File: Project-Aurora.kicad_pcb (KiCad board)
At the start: 4 copper layers, 285 x 94.6 mm, 264 parts, among them P1 USB_OTG, P2 FLASH_HDR, SW1 Reset, SW10 SW_PUSH, SW11 SW_PUSH, SW12 SW_PUSH, SW13 SW_PUSH, SW14 SW_PUSH, SW15 SW_PUSH, SW16 SW_PUSH, SW17 SW_PUSH, SW18 SW_PUSH, SW19 SW_PUSH, SW2 SW_PUSH, SW20 SW_PUSH, SW21 SW_PUSH, SW22 SW_PUSH, SW23 SW_PUSH, SW24 SW_PUSH, SW25 SW_PUSH, SW26 SW_PUSH, SW27 SW_PUSH, SW28 SW_PUSH, SW29 SW_PUSH, SW3 SW_PUSH, SW30 SW_PUSH, SW31 SW_PUSH, SW32 SW_PUSH, SW33 SW_PUSH, SW34 SW_PUSH, SW35 SW_PUSH, SW36 SW_PUSH, SW37 SW_PUSH, SW38 SW_PUSH, SW39 SW_PUSH, SW4 SW_PUSH, SW40 SW_PUSH, SW41 SW_PUSH, SW42 SW_PUSH, SW43 SW_PUSH, SW44 SW_PUSH, SW45 SW_PUSH, SW46 SW_PUSH, SW47 SW_PUSH, SW48 SW_PUSH, SW49 SW_PUSH, SW5 SW_PUSH, SW50 SW_PUSH, SW51 SW_PUSH, SW52 SW_PUSH, SW53 SW_PUSH, SW54 SW_PUSH, SW55 SW_PUSH, SW56 SW_PUSH, SW57 SW_PUSH, SW58 SW_PUSH, SW59 SW_PUSH, SW6 SW_PUSH, SW60 SW_PUSH, SW61 SW_PUSH, SW62 SW_PUSH, SW63 SW_PUSH, SW64 SW_PUSH, SW65 SW_PUSH, SW66 SW_PUSH, SW7 SW_PUSH, SW8 SW_PUSH, SW9 SW_PUSH, U1 MK20DX256VLH7, U2 IS31FL3732, U3 IS31FL3732, U6 Case-Ground, X1 CRYSTAL_SMD

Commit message: Did some visual cleanup.
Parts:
- moved FID1 24.4 mm to (66.0, 83.8)
- moved FID2 24.4 mm to (66.0, 83.8)
- moved D126 10.9 mm to (321.1, 121.4), turned to 0 degrees
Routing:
- net /Keymatrix/Row4Col14: track 19.8 -> 4.89 mm
- net /Keymatrix/Row4: track 307.5 -> 296.7 mm
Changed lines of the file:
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@@
     (thickness 1.6002)
     (drawings 3814)
-    (tracks 2956)
+    (tracks 2954)
     (zones 0)
     (modules 264)
@@
   )
   (module Fiducials:Fiducial_1mm_Dia_2.54mm_Outer_CopperBottom (layer Front)
-    (at 90.424 83.82)
+    (at 66.04 83.82)
     (descr "Circular Fiducial, 1mm bare copper bottom; 2.54mm keepout")
     (tags marker)
@@
   )
   (module Fiducials:Fiducial_1mm_Dia_2.54mm_Outer_CopperTop (layer Front)
-    (at 90.424 83.82)
+    (at 66.04 83.82)
     (descr "Circular Fiducial, 1mm bare copper top; 2.54mm keepout")
     (tags marker)
@@
   (module Keyboard_Stuff:RGB (layer Front)
     (at 326.212 111.85 180)
-    (fp_text reference D1 (at -3.048 2.032 180) (layer F.SilkS)
+    (fp_text reference D1 (at 2.616 2.122 180) (layer F.SilkS)
       (effects (font (size 1 1) (thickness 0.125)))
     )
@@
   (module Keyboard_Stuff:RGB (layer Front)
     (at 161.544 154.874 180)
-    (fp_text reference D21 (at -1.016 3.236 180) (layer F.SilkS)
+    (fp_text reference D21 (at 0 7.046 180) (layer F.SilkS)
       (effects (font (size 1 1) (thickness 0.125)))
     )
@@
     (tags SOD-123)
     (attr smd)
-    (fp_text reference D89 (at 4.064 0 90) (layer F.SilkS)
+    (fp_text reference D89 (at -3.048 0 180) (layer F.SilkS)
       (effects (font (size 1 1) (thickness 0.15)))
     )
@@
     (tags SOD-123)
     (attr smd)
-    (fp_text reference D95 (at 4.064 0 90) (layer F.SilkS)
+    (fp_text reference D95 (at -0.254 -3.302 90) (layer F.SilkS)
       (effects (font (size 1 1) (thickness 0.15)))
     )
@@
     (tags SOD-123)
     (attr smd)
-    (fp_text reference D112 (at 4.064 0) (layer F.SilkS)
+    (fp_text reference D112 (at -4.318 0) (layer F.SilkS)
       (effects (font (size 1 1) (thickness 0.15)))
     )
@@
     (tags SOD-123)
     (attr smd)
-    (fp_text reference D119 (at 4.064 0 90) (layer F.SilkS)
+    (fp_text reference D119 (at -3.302 -1.016 180) (layer F.SilkS)
       (effects (font (size 1 1) (thickness 0.15)))
     )
@@
     (tags SOD-123)
     (attr smd)
-    (fp_text reference D124 (at 4.064 0) (layer F.SilkS)
+    (fp_text reference D124 (at 0.254 2.032) (layer F.SilkS)
       (effects (font (size 1 1) (thickness 0.15)))
     )
@@
   )
   (module Keyboard_Stuff:SOD-123 (layer Front)
-    (at 331.216 125.476 270)
+    (at 321.056 121.412)
     (descr SOD-123)
     (tags SOD-123)
     (attr smd)
-    (fp_text reference D126 (at 4.064 0 270) (layer F.SilkS)
+    (fp_text reference D126 (at 4.064 0) (layer F.SilkS)
       (effects (font (size 1 1) (thickness 0.15)))
     )
-    (fp_text value D (at 0 2.1 270) (layer F.Fab)
+    (fp_text value D (at 0 2.1) (layer F.Fab)
       (effects (font (size 1 1) (thickness 0.15)))
     )
@@
     (fp_line (start -2 0.9) (end 1.54 0.9) (layer F.SilkS) (width 0.15))
     (fp_line (start -2 -0.9) (end 1.54 -0.9) (layer F.SilkS) (width 0.15))
-    (pad 1 smd rect (at -1.635 0 270) (size 0.91 1.22) (layers Front F.Paste F.Mask)
+    (pad 1 smd rect (at -1.635 0) (size 0.91 1.22) (layers Front F.Paste F.Mask)
       (net 55 /Keymatrix/Row4))
-    (pad 2 smd rect (at 1.635 0 270) (size 0.91 1.22) (layers Front F.Paste F.Mask)
+    (pad 2 smd rect (at 1.635 0) (size 0.91 1.22) (layers Front F.Paste F.Mask)
       (net 124 /Keymatrix/Row4Col14))
   )
@@
   (module Keyboard_Stuff:RGB (layer Front)
     (at 314.306 111.85 180)
-    (fp_text reference D129 (at -3.048 2.032 180) (layer F.SilkS)
+    (fp_text reference D129 (at 4.426 2.122 180) (layer F.SilkS)
       (effects (font (size 1 1) (thickness 0.125)))
     )
@@
   (segment (start 147.574 99.933) (end 128.524 99.933) (width 0.19) (layer Front) (net 54) (status 30))
   (segment (start 128.524 99.933) (end 109.474 99.933) (width 0.19) (layer Front) (net 54) (status 30))
+  (segment (start 311.912 123.841) (end 316.992 123.841) (width 0.19) (layer Front) (net 55))
+  (segment (start 316.992 123.841) (end 319.421 121.412) (width 0.19) (layer Front) (net 55))
   (via (at 114.3 123.952) (size 0.6) (layers Front Back) (net 55))
   (segment (start 132.142 150.43) (end 137.156 150.43) (width 0.19) (layer Back) (net 55) (status 20))
@@
   (segment (start 105.156 140.716) (end 107.188 138.684) (width 0.19) (layer Front) (net 55))
   (segment (start 102.163 140.716) (end 105.156 140.716) (width 0.19) (layer Front) (net 55))
-  (segment (start 311.912 123.841) (end 331.216 123.841) (width 0.19) (layer Front) (net 55) (status 30))
   (segment (start 102.108 140.716) (end 102.163 140.716) (width 0.19) (layer Front) (net 55))
   (segment (start 276.352 123.841) (end 311.912 123.841) (width 0.19) (layer Front) (net 55) (status 30))
@@
   (segment (start 326.157 97.88) (end 324.469 99.568) (width 0.19) (layer Front) (net 123) (status 20))
   (segment (start 330.816 97.88) (end 326.157 97.88) (width 0.19) (layer Front) (net 123) (status 10))
-  (segment (start 332.121 127.111) (end 331.216 127.111) (width 0.19) (layer Front) (net 124) (status 20))
-  (segment (start 333.756 125.476) (end 332.121 127.111) (width 0.19) (layer Front) (net 124))
-  (segment (start 333.756 120.396) (end 333.756 125.476) (width 0.19) (layer Front) (net 124))
-  (segment (start 330.29 116.93) (end 333.756 120.396) (width 0.19) (layer Front) (net 124))
-  (segment (start 323.672 116.93) (end 330.29 116.93) (width 0.19) (layer Front) (net 124) (status 10))
+  (segment (start 323.672 116.93) (end 323.672 120.431) (width 0.19) (layer Front) (net 124))
+  (segment (start 323.672 120.431) (end 322.691 121.412) (width 0.19) (layer Front) (net 124))
   (segment (start 327.353 155.03) (end 326.136 153.813) (width 0.19) (layer Front) (net 125) (status 20))
   (segment (start 333.197 155.03) (end 327.353 155.03) (width 0.19) (layer Front) (net 125) (status 10))

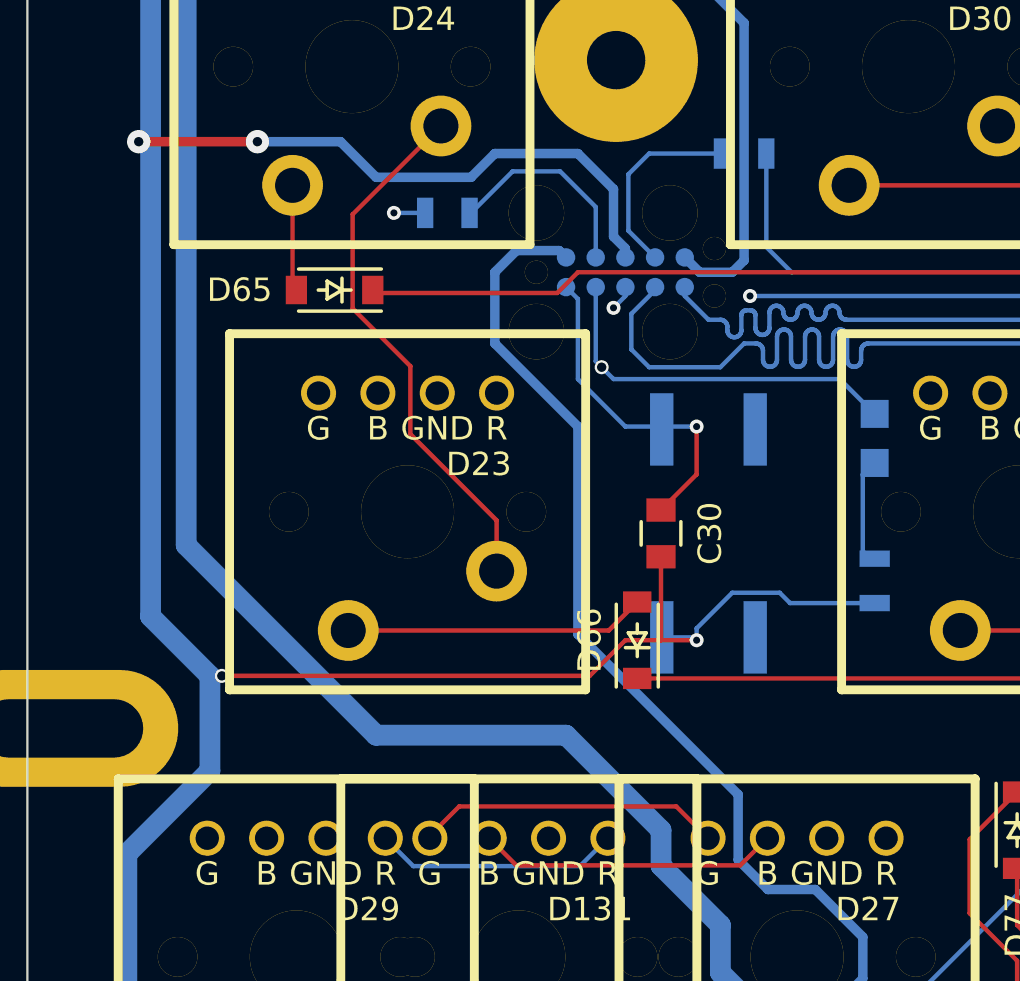
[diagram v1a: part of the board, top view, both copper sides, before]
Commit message: Added Debug-Port
In order to avoid buying the JLink Needle.
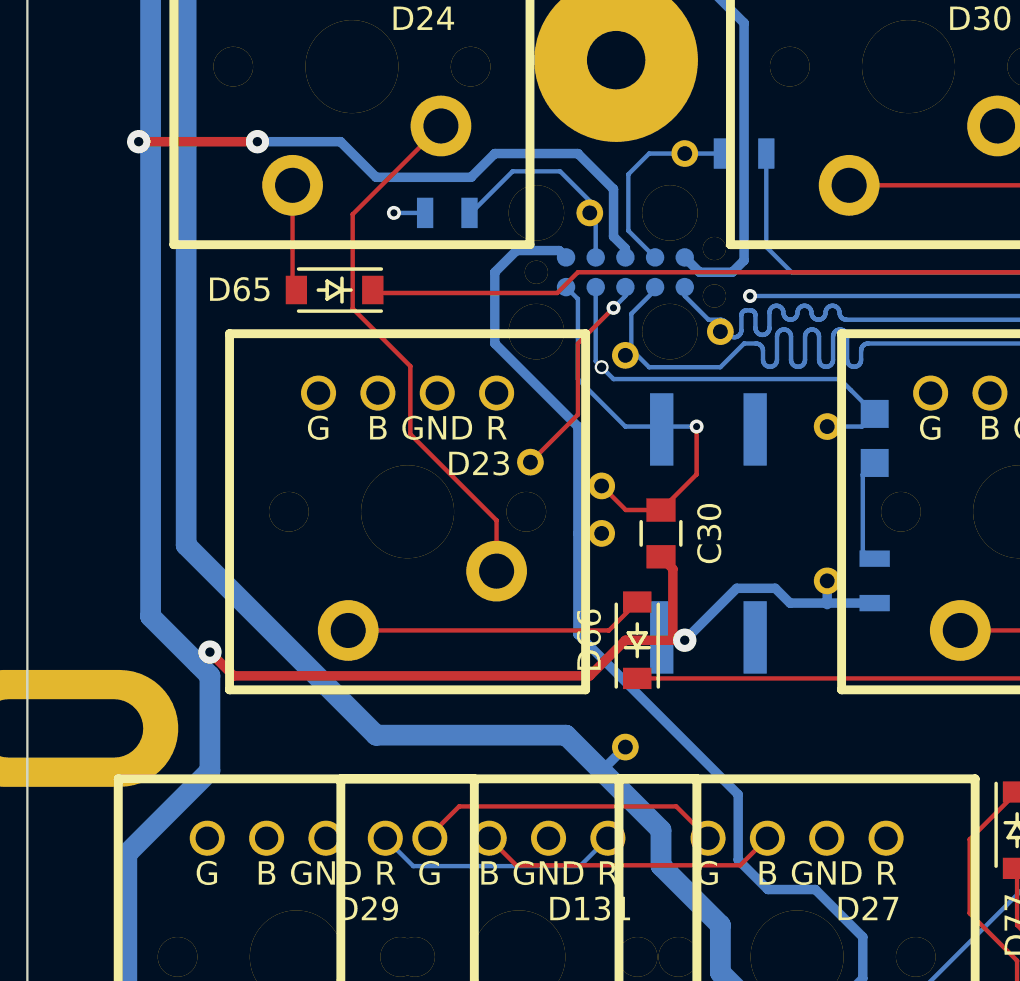
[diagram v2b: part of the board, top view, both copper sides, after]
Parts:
- added P10: DBG, Connect:PINTST, B.Cu at (83.8, 109.7)
- added P11: DBG, Connect:PINTST, B.Cu at (87.9, 105.2)
- added P12: DBG, Connect:PINTST, B.Cu at (91.9, 104.1)
- added P3: DBG, Connect:PINTST, B.Cu at (86.9, 112.8)
- added P4: DBG, Connect:PINTST, B.Cu at (86.4, 99.1)
- added P5: DBG, Connect:PINTST, B.Cu at (96.5, 114.8)
- added P6: DBG, Connect:PINTST, B.Cu at (90.4, 96.5)
- added P7: DBG, Connect:PINTST, B.Cu at (87.9, 121.9)
- added P8: DBG, Connect:PINTST, B.Cu at (86.9, 110.7)
- added P9: DBG, Connect:PINTST, B.Cu at (96.5, 108.2)
- C30: value 100n -> 0.1uF
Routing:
- net /RX0: track 93.4 -> 101.5 mm
- net GND: track 307.8 -> 311.7 mm
- net /MCU_RESET: track 105.3 -> 108.3 mm
- net /PTA5: track 111.1 -> 113.4 mm
- net +5V: track 439.0 -> 440.4 mm
- net +3V3: track 265.0 -> 266.0 mm
- net /SWD_DIO: track 8.93 -> 9.43 mm
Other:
- board text added: "3.3V"
- board text added: "5V"
- board text added: "GND"
- board text added: "PTA5"
- board text added: "RX0"
- board text added: "Reset"
- board text added: "SWD_CLK"
- board text added: "SWD_IO"
- board text added: "TX0"
- board text added: "TX1"

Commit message: Switched to a different USB Port and 100uF Cap
also added a USB-Debug Header and did some cleanup
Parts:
- added P13: CONN_01X04, Pin_Headers:Pin_Header_Straight_1x04_Pitch2.00mm, F.Cu at (99.9, 82.2)
- C10: renamed from C5; value 1uF -> 0.1uF
- C20: footprint Capacitors_SMD:C_0805 -> Capacitors_SMD:C_1206
- C5: renamed from C9; value 0.1uF -> 1uF
- C6: renamed from C10; value 0.1uF -> 1uF
- C9: renamed from C6; value 1uF -> 0.1uF
- D1, D10, D11, D12, D129, D13, D130, D131, D14, D15, D16, D17, D18, D19, D2, D20, D21, D22, D23, D24, D25, D26, D27, D28, D29, D3, D30, D31, D32, D33, D34, D35, D36, D37, D38, D39, D4, D40, D41, D42, D43, D44, D45, D46, D47, D48, D49, D5, D50, D51, D52, D53, D54, D55, D56, D57, D58, D59, D6, D60, D61, D62, D63, D64, D7, D8, D9: footprint Keyboard_Stuff:RGB -> libs.pretty:RGB
- D100, D101, D102, D103, D104, D105, D106, D107, D108, D109, D110, D111, D112, D113, D114, D115, D116, D117, D118, D119, D120, D121, D122, D123, D124, D126, D127, D128, D65, D66, D67, D68, D69, D70, D71, D72, D73, D74, D75, D76, D77, D78, D79, D80, D81, D82, D83, D84, D85, D86, D87, D88, D89, D90, D91, D92, D93, D94, D95, D96, D97, D98, D99: footprint Keyboard_Stuff:SOD-123 -> libs.pretty:SOD-123
- P1: footprint Connect:USB_Micro-B -> libs.pretty:Micro-USB_629105150521
- SW10, SW11, SW12, SW13, SW14, SW15, SW16, SW17, SW18, SW19, SW2, SW20, SW21, SW22, SW23, SW24, SW25, SW26, SW27, SW28, SW29, SW3, SW30, SW31, SW32, SW33, SW34, SW35, SW36, SW37, SW38, SW39, SW4, SW40, SW41, SW42, SW43, SW44, SW45, SW46, SW47, SW48, SW49, SW5, SW50, SW51, SW52, SW53, SW54, SW55, SW56, SW57, SW58, SW59, SW6, SW60, SW61, SW62, SW63, SW64, SW65, SW66, SW7, SW8, SW9: footprint Keyboard_Stuff:MX1A -> libs.pretty:MX1A
- moved R5 6.62 mm to (104.4, 81.5)
- moved R6 6.39 mm to (105.4, 83.7)
- moved D74 6.13 mm to (95.2, 83.2), turned to 180 degrees
- moved C20 3.75 mm to (82.3, 74.2), turned to 270 degrees
- moved P1 2.67 mm to (80.5, 64.6)
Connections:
- net Net-(P1-Pad2) renamed /D-5V
- net Net-(P1-Pad3) renamed /D+5V
- P1 pad 4: Net-(P1-Pad4) -> (no net)
- U1 pad 1: Net-(U1-Pad1) -> (no net)
- U1 pad 10: Net-(U1-Pad10) -> (no net)
- U1 pad 11: Net-(U1-Pad11) -> (no net)
- U1 pad 12: Net-(U1-Pad12) -> (no net)
- U1 pad 13: Net-(U1-Pad13) -> (no net)
- U1 pad 14: Net-(U1-Pad14) -> (no net)
- U1 pad 15: Net-(U1-Pad15) -> (no net)
- U1 pad 16: Net-(U1-Pad16) -> (no net)
- U1 pad 17: Net-(U1-Pad17) -> (no net)
- U1 pad 18: Net-(U1-Pad18) -> (no net)
- U1 pad 19: Net-(U1-Pad19) -> (no net)
- U1 pad 2: Net-(U1-Pad2) -> (no net)
- U1 pad 20: Net-(U1-Pad20) -> (no net)
- U1 pad 39: Net-(U1-Pad39) -> (no net)
- U1 pad 40: Net-(U1-Pad40) -> (no net)
- U1 pad 41: Net-(U1-Pad41) -> (no net)
- U1 pad 42: Net-(U1-Pad42) -> (no net)
- U1 pad 43: Net-(U1-Pad43) -> (no net)
- U1 pad 44: Net-(U1-Pad44) -> (no net)
- U1 pad 45: Net-(U1-Pad45) -> (no net)
- U1 pad 9: Net-(U1-Pad9) -> (no net)
- U2 pad 10: Net-(U2-Pad10) -> (no net)
- U2 pad 2: Net-(U2-Pad2) -> (no net)
- U2 pad 3: Net-(U2-Pad3) -> (no net)
- U2 pad 5: Net-(U2-Pad5) -> (no net)
- U2 pad 6: Net-(U2-Pad6) -> (no net)
- U3 pad 10: Net-(U3-Pad10) -> (no net)
- U3 pad 2: Net-(U3-Pad2) -> (no net)
- U3 pad 3: Net-(U3-Pad3) -> (no net)
- U3 pad 6: Net-(U3-Pad6) -> (no net)
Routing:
- net +5V: track 440.4 -> 456.8 mm
- net GND: track 311.7 -> 300.4 mm, vias 37 -> 33
- net /LED2B/CB2: track 267.8 -> 275.7 mm
- net /D+: track 88.1 -> 81.9 mm
- net /D-: track 85.2 -> 79.4 mm
- net /LED2B/CB8: track 312.5 -> 318.0 mm
- net /Keymatrix/Row1Col2: track 12.5 -> 7.49 mm
- net /D+5V: track 24.3 -> 29.2 mm
- net /LED1A/CA3: track 231.0 -> 235.9 mm
- net /Keymatrix/Row1: track 371.5 -> 375.5 mm
- net /D-5V: track 28.2 -> 31.9 mm
- net /LED2B/CB7: track 308.7 -> 311.2 mm
- net /Keymatrix/Row1Col1: track 12.7 -> 15.2 mm, vias 0 -> 1
